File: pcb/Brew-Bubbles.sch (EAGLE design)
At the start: 7 parts, among them U1 GP1A57HR

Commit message: JsonConfig working (mostly)
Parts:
- renumbered AMBIENT to ROOM
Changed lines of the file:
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@@
 <drawing>
 <settings>
-<setting alwaysvectorfont="yes"/>
+<setting alwaysvectorfont="no"/>
 <setting verticaltext="up"/>
 </settings>
@@
 </classes>
 <parts>
-<part name="AMBIENT" library="SparkFun-Sensors" deviceset="DS18B20" device=""/>
+<part name="ROOM" library="SparkFun-Sensors" deviceset="DS18B20" device=""/>
 <part name="U$2" library="diy-modules" deviceset="WEMOS-D1-MINI-SHIELD" device=""/>
 <part name="R1" library="SparkFun-Resistors" library_urn="urn:adsk.eagle:library:532" deviceset="330OHM" device="-HORIZ-1/10W-5%" package3d_urn="urn:adsk.eagle:package:39658/1" value="2.2kΩ"/>
@@
 </plain>
 <instances>
-<instance part="AMBIENT" gate="G$1" x="-10.16" y="52.07" smashed="yes" rot="R270">
+<instance part="ROOM" gate="G$1" x="-10.16" y="52.07" smashed="yes" rot="R270">
 <attribute name="NAME" x="-14.986" y="44.45" size="1.778" layer="95" font="vector"/>
 <attribute name="VALUE" x="-15.494" y="43.18" size="1.778" layer="96" font="vector" align="top-left"/>
@@
 <wire x1="-7.62" y1="87.63" x2="33.02" y2="87.63" width="0.1524" layer="91"/>
 <junction x="33.02" y="87.63"/>
-<pinref part="AMBIENT" gate="G$1" pin="VDD"/>
+<pinref part="ROOM" gate="G$1" pin="VDD"/>
 <wire x1="-5.08" y1="62.23" x2="-5.08" y2="64.77" width="0.1524" layer="91"/>
 <wire x1="-5.08" y1="64.77" x2="33.02" y2="64.77" width="0.1524" layer="91"/>
@@
 <pinref part="R1" gate="G$1" pin="1"/>
 <wire x1="1.27" y1="71.12" x2="-10.16" y2="71.12" width="0.1524" layer="91"/>
-<pinref part="AMBIENT" gate="G$1" pin="DQ"/>
+<pinref part="ROOM" gate="G$1" pin="DQ"/>
 <wire x1="-10.16" y1="71.12" x2="-10.16" y2="62.23" width="0.1524" layer="91"/>
 <wire x1="-10.16" y1="71.12" x2="-27.94" y2="71.12" width="0.1524" layer="91"/>
@@
 <wire x1="-12.7" y1="96.52" x2="-12.7" y2="85.09" width="0.1524" layer="91"/>
 <wire x1="-12.7" y1="85.09" x2="-15.24" y2="85.09" width="0.1524" layer="91"/>
-<pinref part="AMBIENT" gate="G$1" pin="GND"/>
+<pinref part="ROOM" gate="G$1" pin="GND"/>
 <wire x1="-15.24" y1="85.09" x2="-15.24" y2="64.77" width="0.1524" layer="91"/>
 <wire x1="-15.24" y1="64.77" x2="-15.24" y2="62.23" width="0.1524" layer="91"/>

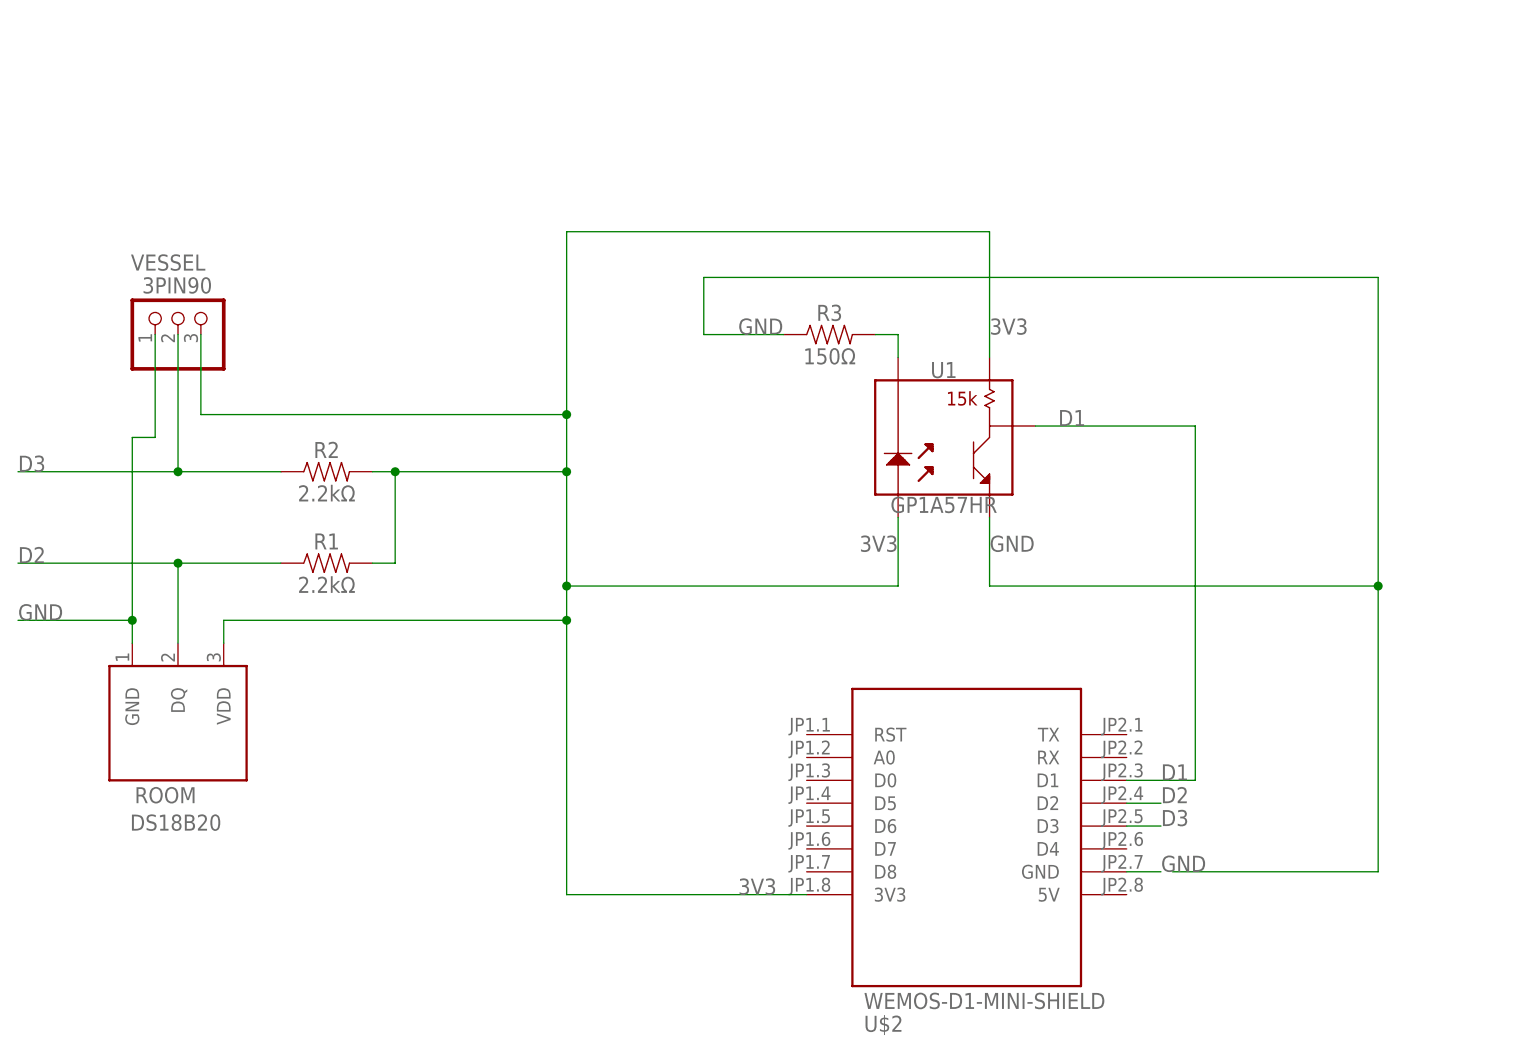
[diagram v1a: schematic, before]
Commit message: Update PCB, add README
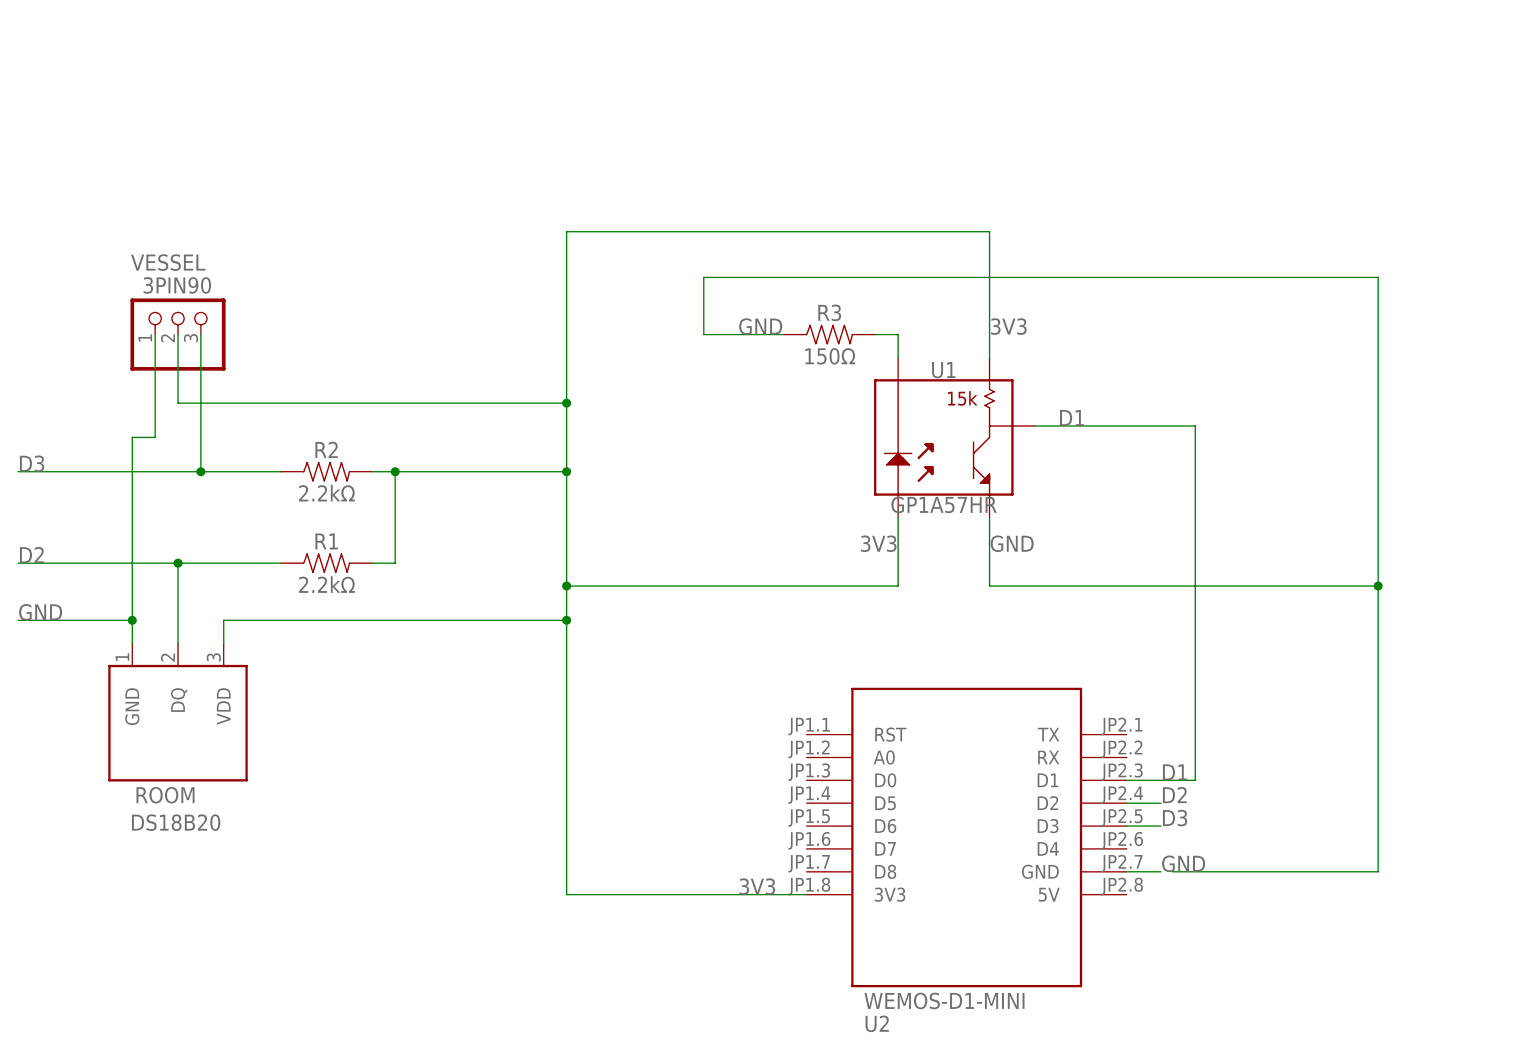
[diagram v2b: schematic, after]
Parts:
- U2: value WEMOS-D1-MINI-SHIELD -> WEMOS-D1-MINI
- renumbered U$2 to U2
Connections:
- net 3V3: now also VESSEL.2; no longer VESSEL.3
- net D3: now also VESSEL.3; no longer VESSEL.2
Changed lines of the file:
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@@
 <drawing>
 <settings>
-<setting alwaysvectorfont="no"/>
+<setting alwaysvectorfont="yes"/>
 <setting verticaltext="up"/>
 </settings>
@@
 <parts>
 <part name="ROOM" library="SparkFun-Sensors" deviceset="DS18B20" device=""/>
-<part name="U$2" library="diy-modules" deviceset="WEMOS-D1-MINI-SHIELD" device=""/>
+<part name="U2" library="diy-modules" deviceset="WEMOS-D1-MINI-SHIELD" device="" value="WEMOS-D1-MINI"/>
 <part name="R1" library="SparkFun-Resistors" library_urn="urn:adsk.eagle:library:532" deviceset="330OHM" device="-HORIZ-1/10W-5%" package3d_urn="urn:adsk.eagle:package:39658/1" value="2.2kΩ"/>
 <part name="VESSEL" library="pinhead" library_urn="urn:adsk.eagle:library:325" deviceset="PINHD-1X3" device="/90" package3d_urn="urn:adsk.eagle:package:22459/2" value="3PIN90"/>
@@
 <attribute name="VALUE" x="-15.494" y="43.18" size="1.778" layer="96" font="vector" align="top-left"/>
 </instance>
-<instance part="U$2" gate="G$1" x="77.47" y="41.91" smashed="yes">
+<instance part="U2" gate="G$1" x="77.47" y="41.91" smashed="yes">
 <attribute name="NAME" x="66.04" y="19.05" size="1.778" layer="95"/>
 <attribute name="VALUE" x="66.04" y="21.59" size="1.778" layer="96"/>
@@
 <label x="69.85" y="72.39" size="1.778" layer="95" align="bottom-right"/>
 <wire x1="69.85" y1="76.2" x2="69.85" y2="68.58" width="0.1524" layer="91"/>
-<pinref part="U$2" gate="G$1" pin="3V3"/>
+<pinref part="U2" gate="G$1" pin="3V3"/>
 <label x="52.07" y="34.29" size="1.778" layer="95"/>
 <wire x1="59.69" y1="34.29" x2="33.02" y2="34.29" width="0.1524" layer="91"/>
@@
 <wire x1="33.02" y1="64.77" x2="33.02" y2="68.58" width="0.1524" layer="91"/>
 <wire x1="33.02" y1="68.58" x2="33.02" y2="81.28" width="0.1524" layer="91"/>
-<wire x1="33.02" y1="81.28" x2="33.02" y2="87.63" width="0.1524" layer="91"/>
-<wire x1="33.02" y1="87.63" x2="33.02" y2="107.95" width="0.1524" layer="91"/>
+<wire x1="33.02" y1="81.28" x2="33.02" y2="88.9" width="0.1524" layer="91"/>
+<wire x1="33.02" y1="88.9" x2="33.02" y2="107.95" width="0.1524" layer="91"/>
 <wire x1="69.85" y1="68.58" x2="33.02" y2="68.58" width="0.1524" layer="91"/>
 <junction x="33.02" y="68.58"/>
@@
 <junction x="13.97" y="81.28"/>
 <junction x="33.02" y="81.28"/>
-<pinref part="VESSEL" gate="A" pin="3"/>
-<wire x1="-7.62" y1="96.52" x2="-7.62" y2="87.63" width="0.1524" layer="91"/>
-<wire x1="-7.62" y1="87.63" x2="33.02" y2="87.63" width="0.1524" layer="91"/>
-<junction x="33.02" y="87.63"/>
 <pinref part="ROOM" gate="G$1" pin="VDD"/>
 <wire x1="-5.08" y1="62.23" x2="-5.08" y2="64.77" width="0.1524" layer="91"/>
 <wire x1="-5.08" y1="64.77" x2="33.02" y2="64.77" width="0.1524" layer="91"/>
 <junction x="33.02" y="64.77"/>
+<pinref part="VESSEL" gate="A" pin="2"/>
+<wire x1="-10.16" y1="96.52" x2="-10.16" y2="88.9" width="0.1524" layer="91"/>
+<wire x1="-10.16" y1="88.9" x2="33.02" y2="88.9" width="0.1524" layer="91"/>
+<junction x="33.02" y="88.9"/>
 </segment>
 </net>
 <net name="D2" class="0">
 <segment>
-<pinref part="U$2" gate="G$1" pin="D2"/>
+<pinref part="U2" gate="G$1" pin="D2"/>
 <label x="99.06" y="44.45" size="1.778" layer="95"/>
 <wire x1="99.06" y1="44.45" x2="95.25" y2="44.45" width="0.1524" layer="91"/>
@@
 <net name="D3" class="0">
 <segment>
-<pinref part="U$2" gate="G$1" pin="D3"/>
+<pinref part="U2" gate="G$1" pin="D3"/>
 <label x="99.06" y="41.91" size="1.778" layer="95"/>
 <wire x1="99.06" y1="41.91" x2="95.25" y2="41.91" width="0.1524" layer="91"/>
 </segment>
 <segment>
-<wire x1="-10.16" y1="96.52" x2="-10.16" y2="81.28" width="0.1524" layer="91"/>
 <pinref part="R2" gate="G$1" pin="1"/>
-<wire x1="-10.16" y1="81.28" x2="1.27" y2="81.28" width="0.1524" layer="91"/>
-<pinref part="VESSEL" gate="A" pin="2"/>
-<wire x1="-10.16" y1="81.28" x2="-27.94" y2="81.28" width="0.1524" layer="91"/>
-<junction x="-10.16" y="81.28"/>
+<wire x1="1.27" y1="81.28" x2="-7.62" y2="81.28" width="0.1524" layer="91"/>
 <label x="-27.94" y="81.28" size="1.778" layer="95"/>
+<pinref part="VESSEL" gate="A" pin="3"/>
+<wire x1="-7.62" y1="81.28" x2="-27.94" y2="81.28" width="0.1524" layer="91"/>
+<wire x1="-7.62" y1="96.52" x2="-7.62" y2="81.28" width="0.1524" layer="91"/>
+<junction x="-7.62" y="81.28"/>
 </segment>
 </net>
 <net name="GND" class="0">
 <segment>
-<pinref part="U$2" gate="G$1" pin="GND"/>
+<pinref part="U2" gate="G$1" pin="GND"/>
 <wire x1="95.25" y1="36.83" x2="99.06" y2="36.83" width="0.1524" layer="91"/>
 <label x="99.06" y="36.83" size="1.778" layer="95"/>
@@
 <net name="D1" class="0">
 <segment>
-<pinref part="U$2" gate="G$1" pin="D1"/>
+<pinref part="U2" gate="G$1" pin="D1"/>
 <wire x1="95.25" y1="46.99" x2="102.87" y2="46.99" width="0.1524" layer="91"/>
 <label x="99.06" y="46.99" size="1.778" layer="95"/>

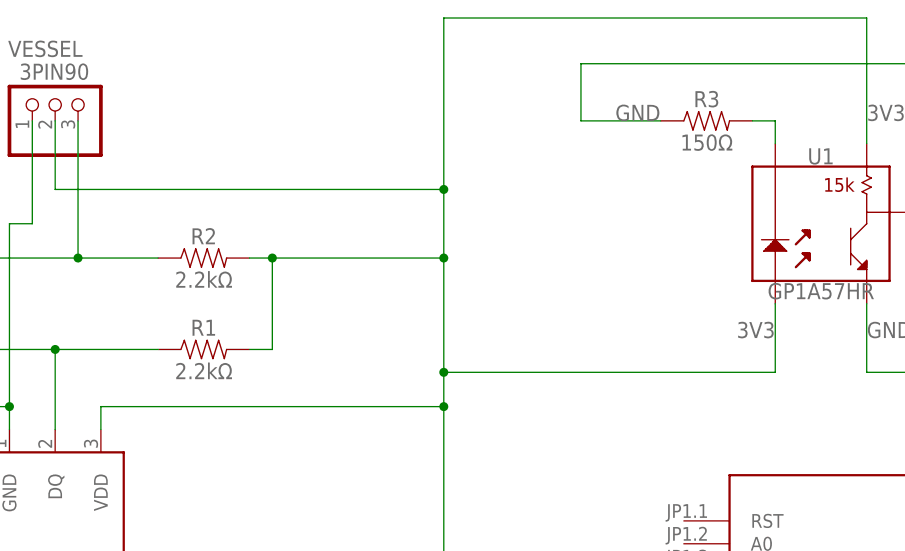
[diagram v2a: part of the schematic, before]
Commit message: Update PCD, remove acid traps
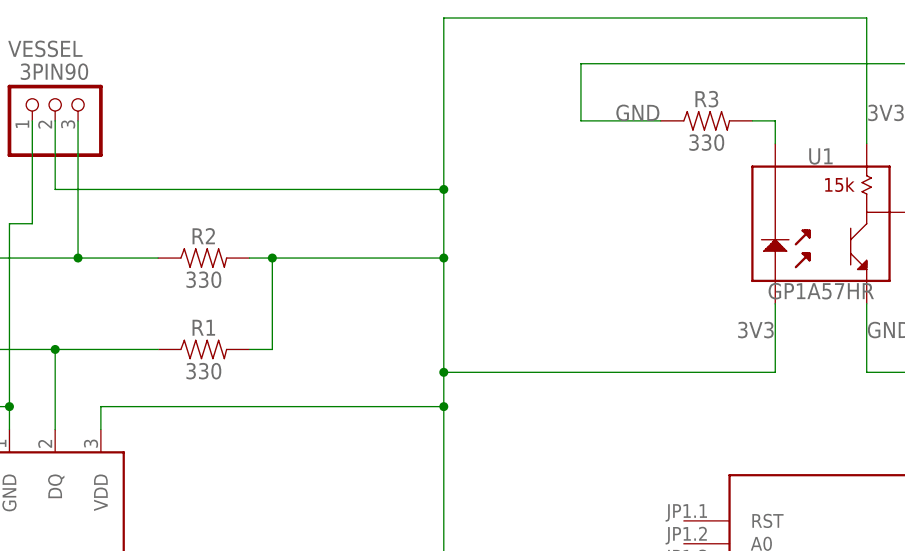
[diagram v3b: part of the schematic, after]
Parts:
- R1, R2: value 2.2kΩ -> 330
- R3: value 150Ω -> 330
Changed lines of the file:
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@@
 <drawing>
 <settings>
-<setting alwaysvectorfont="yes"/>
+<setting alwaysvectorfont="no"/>
 <setting verticaltext="up"/>
 </settings>
@@
 <part name="ROOM" library="SparkFun-Sensors" deviceset="DS18B20" device=""/>
 <part name="U2" library="diy-modules" deviceset="WEMOS-D1-MINI-SHIELD" device="" value="WEMOS-D1-MINI"/>
-<part name="R1" library="SparkFun-Resistors" library_urn="urn:adsk.eagle:library:532" deviceset="330OHM" device="-HORIZ-1/10W-5%" package3d_urn="urn:adsk.eagle:package:39658/1" value="2.2kΩ"/>
+<part name="R1" library="SparkFun-Resistors" deviceset="330OHM" device="-HORIZ-1/10W-5%" value="330"/>
 <part name="VESSEL" library="pinhead" library_urn="urn:adsk.eagle:library:325" deviceset="PINHD-1X3" device="/90" package3d_urn="urn:adsk.eagle:package:22459/2" value="3PIN90"/>
-<part name="R2" library="SparkFun-Resistors" library_urn="urn:adsk.eagle:library:532" deviceset="330OHM" device="-HORIZ-1/10W-5%" package3d_urn="urn:adsk.eagle:package:39658/1" value="2.2kΩ"/>
+<part name="R2" library="SparkFun-Resistors" deviceset="330OHM" device="-HORIZ-1/10W-5%" value="330"/>
 <part name="U1" library="SparkFun-Sensors" deviceset="GP1A57HR" device=""/>
-<part name="R3" library="SparkFun-Resistors" library_urn="urn:adsk.eagle:library:532" deviceset="330OHM" device="-HORIZ-1/10W-5%" package3d_urn="urn:adsk.eagle:package:39658/1" value="150Ω"/>
+<part name="R3" library="SparkFun-Resistors" deviceset="330OHM" device="-HORIZ-1/10W-5%" value="330"/>
 </parts>
 <sheets>

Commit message: Updates to trace routes
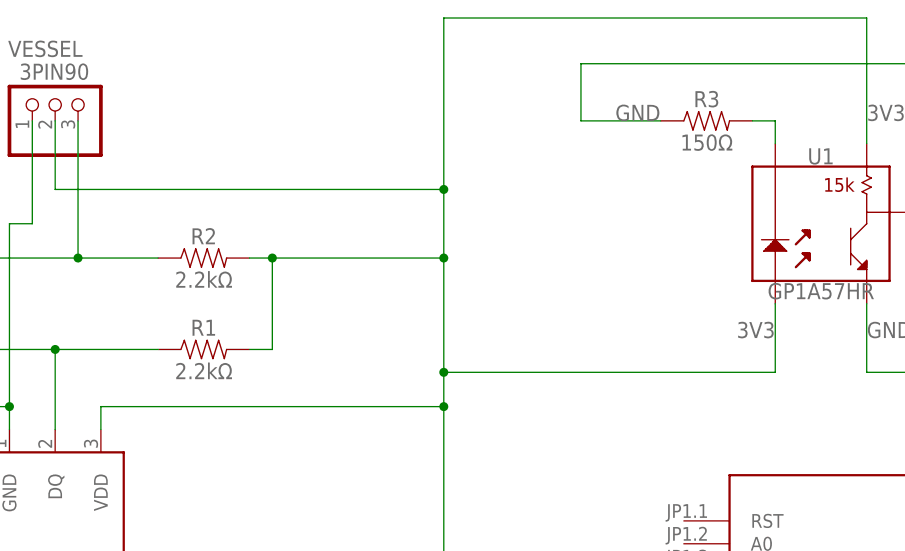
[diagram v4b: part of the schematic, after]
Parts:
- R1, R2: value 330 -> 2.2kΩ
- R3: value 330 -> 150Ω
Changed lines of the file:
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@@
 <drawing>
 <settings>
-<setting alwaysvectorfont="no"/>
+<setting alwaysvectorfont="yes"/>
 <setting verticaltext="up"/>
 </settings>
@@
 <part name="ROOM" library="SparkFun-Sensors" deviceset="DS18B20" device=""/>
 <part name="U2" library="diy-modules" deviceset="WEMOS-D1-MINI-SHIELD" device="" value="WEMOS-D1-MINI"/>
-<part name="R1" library="SparkFun-Resistors" deviceset="330OHM" device="-HORIZ-1/10W-5%" value="330"/>
+<part name="R1" library="SparkFun-Resistors" deviceset="330OHM" device="-HORIZ-1/10W-5%" value="2.2kΩ"/>
 <part name="VESSEL" library="pinhead" library_urn="urn:adsk.eagle:library:325" deviceset="PINHD-1X3" device="/90" package3d_urn="urn:adsk.eagle:package:22459/2" value="3PIN90"/>
-<part name="R2" library="SparkFun-Resistors" deviceset="330OHM" device="-HORIZ-1/10W-5%" value="330"/>
+<part name="R2" library="SparkFun-Resistors" deviceset="330OHM" device="-HORIZ-1/10W-5%" value="2.2kΩ"/>
 <part name="U1" library="SparkFun-Sensors" deviceset="GP1A57HR" device=""/>
-<part name="R3" library="SparkFun-Resistors" deviceset="330OHM" device="-HORIZ-1/10W-5%" value="330"/>
+<part name="R3" library="SparkFun-Resistors" deviceset="330OHM" device="-HORIZ-1/10W-5%" value="150Ω"/>
 </parts>
 <sheets>
